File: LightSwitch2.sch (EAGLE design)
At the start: 3 parts, among them SW1 SWITCH-SPDT-ILLUMINATED, SW2 SWITCH-SPDT-ILLUMINATED

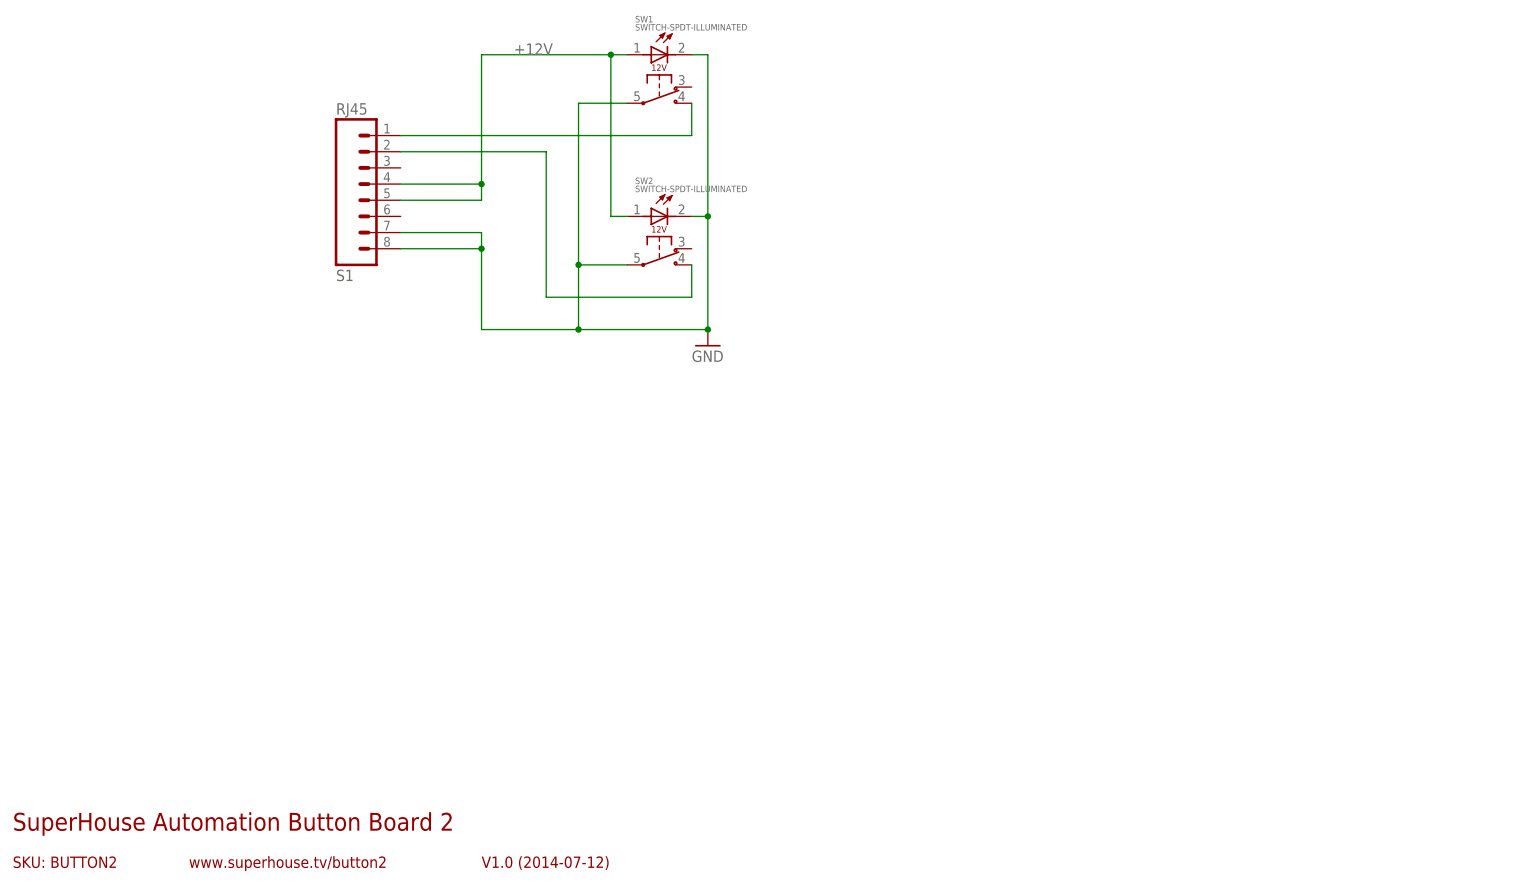
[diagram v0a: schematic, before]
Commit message: Improved labels for clarity
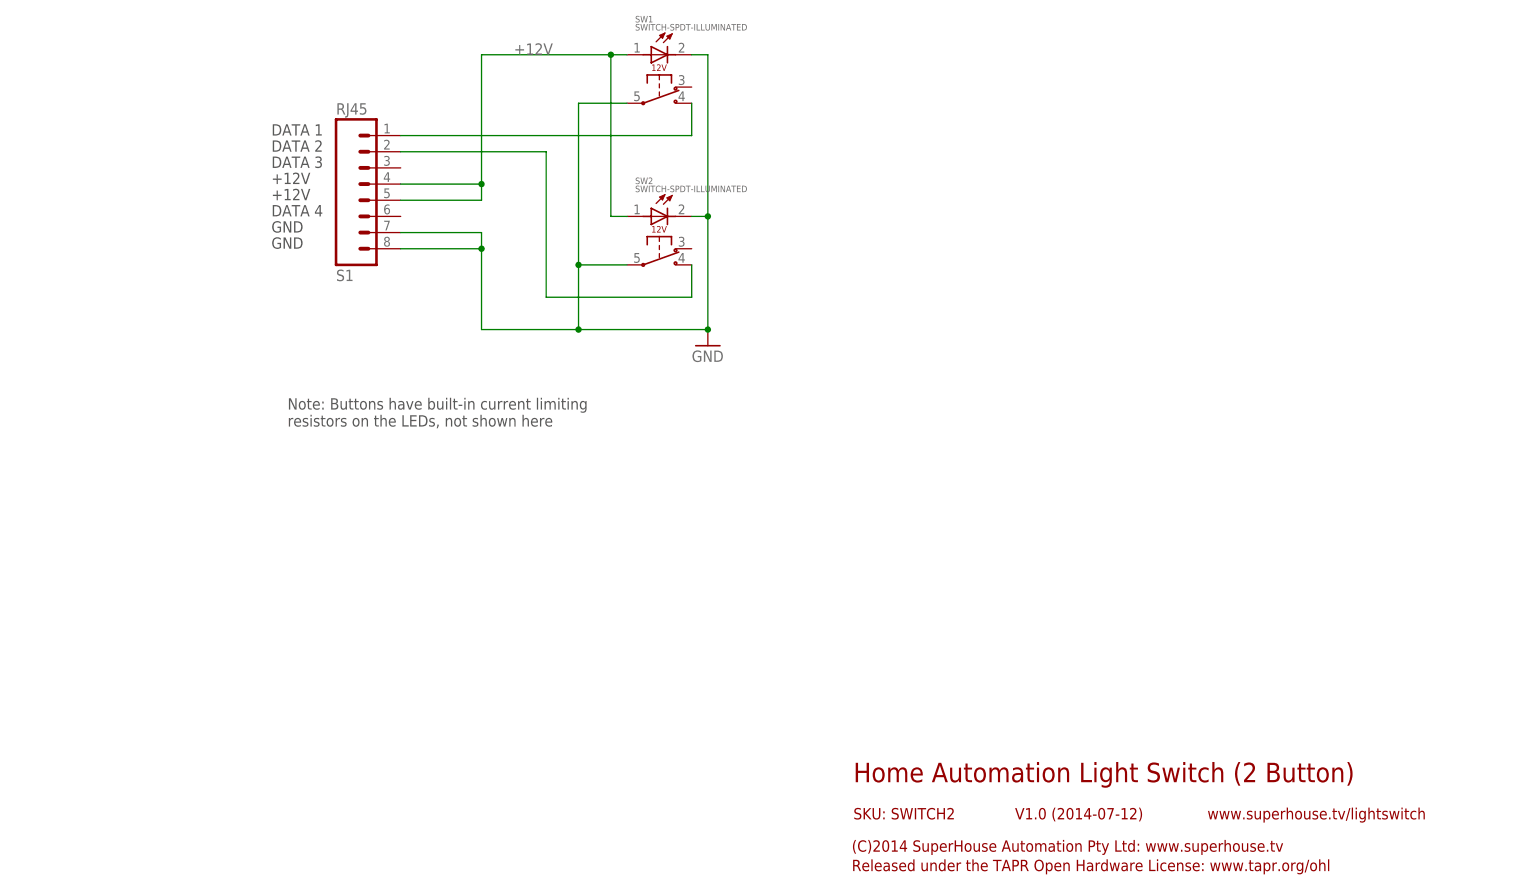
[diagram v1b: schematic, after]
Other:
- note added: "(C)2014 SuperHouse Automation Pty Ltd: www.superhouse.tv"
- note added: "+12V"
- note added: "DATA 1"
- note added: "DATA 2"
- note added: "DATA 3"
- note added: "DATA 4"
- note added: "GND"
- note added: "Home Automation Light Switch (2 Button)"
- note added: "Note: Buttons have built-in current limiting resistors on the LEDs, not shown here"
- note added: "Released under the TAPR Open Hardware License: www.tapr.org/ohl"
- note added: "SKU: SWITCH2"
- note added: "www.superhouse.tv/lightswitch"
- note removed: "SKU: BUTTON2"
- note removed: "SuperHouse Automation Button Board 2"
- note removed: "www.superhouse.tv/button2"
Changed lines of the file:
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@@
 <?xml version="1.0" encoding="utf-8"?>
 <!DOCTYPE eagle SYSTEM "eagle.dtd">
-<eagle version="6.5.0">
+<eagle version="8.3.2">
 <drawing>
 <settings>
 <setting alwaysvectorfont="yes"/>
+<setting keepoldvectorfont="yes"/>
 <setting verticaltext="up"/>
 </settings>
@@
 <sheet>
 <plain>
-<text x="7.62" y="6.858" size="1.778" layer="94">SKU: BUTTON2</text>
-<text x="7.62" y="12.7" size="2.794" layer="94">SuperHouse Automation Button Board 2</text>
-<text x="81.28" y="6.858" size="1.778" layer="94">V1.0 (2014-07-12)</text>
-<text x="35.306" y="6.858" size="1.778" layer="94">www.superhouse.tv/button2</text>
 <frame x1="0" y1="0" x2="248.92" y2="185.42" columns="8" rows="5" layer="94"/>
-<frame x1="5.08" y1="5.08" x2="109.22" y2="17.78" columns="0" rows="0" layer="94" border-left="no" border-top="no" border-right="no" border-bottom="no"/>
-<frame x1="78.74" y1="5.08" x2="109.22" y2="10.16" columns="8" rows="5" layer="94"/>
-<frame x1="5.08" y1="5.08" x2="30.48" y2="10.16" columns="8" rows="5" layer="94"/>
+<text x="139.7" y="20.32" size="3.048" layer="94">Home Automation Light Switch (2 Button)</text>
+<text x="165.1" y="14.478" size="1.778" layer="94">V1.0 (2014-07-12)</text>
+<text x="139.7" y="14.478" size="1.778" layer="94">SKU: SWITCH2</text>
+<text x="139.446" y="9.398" size="1.778" layer="94">(C)2014 SuperHouse Automation Pty Ltd: www.superhouse.tv</text>
+<text x="139.446" y="6.35" size="1.778" layer="94">Released under the TAPR Open Hardware License: www.tapr.org/ohl</text>
+<text x="195.326" y="14.478" size="1.778" layer="94">www.superhouse.tv/lightswitch</text>
+<frame x1="137.16" y1="12.7" x2="243.84" y2="25.4" columns="0" rows="0" layer="94" border-left="no" border-top="no" border-right="no" border-bottom="no"/>
+<frame x1="162.56" y1="12.7" x2="193.04" y2="17.78" columns="8" rows="5" layer="94"/>
+<frame x1="137.16" y1="5.08" x2="243.84" y2="17.78" columns="0" rows="0" layer="94" border-left="no" border-top="no" border-right="no" border-bottom="no"/>
+<text x="48.26" y="121.92" size="1.778" layer="97">DATA 1</text>
+<text x="48.26" y="119.38" size="1.778" layer="97">DATA 2</text>
+<text x="48.26" y="116.84" size="1.778" layer="97">DATA 3</text>
+<text x="48.26" y="109.22" size="1.778" layer="97">DATA 4</text>
+<text x="48.26" y="114.3" size="1.778" layer="97">+12V</text>
+<text x="48.26" y="111.76" size="1.778" layer="97">+12V</text>
+<text x="48.26" y="106.68" size="1.778" layer="97">GND</text>
+<text x="48.26" y="104.14" size="1.778" layer="97">GND</text>
+<text x="50.8" y="76.2" size="1.778" layer="97">Note: Buttons have built-in current limiting
+resistors on the LEDs, not shown here</text>
 </plain>
 <instances>
@@
 </schematic>
 </drawing>
+<compatibility>
+<note version="6.3" minversion="6.2.2" severity="warning">
+Since Version 6.2.2 text objects can contain more than one line,
+which will not be processed correctly with this version.
+</note>
+</compatibility>
 </eagle>

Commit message: Replaced buttons with more common SPST type
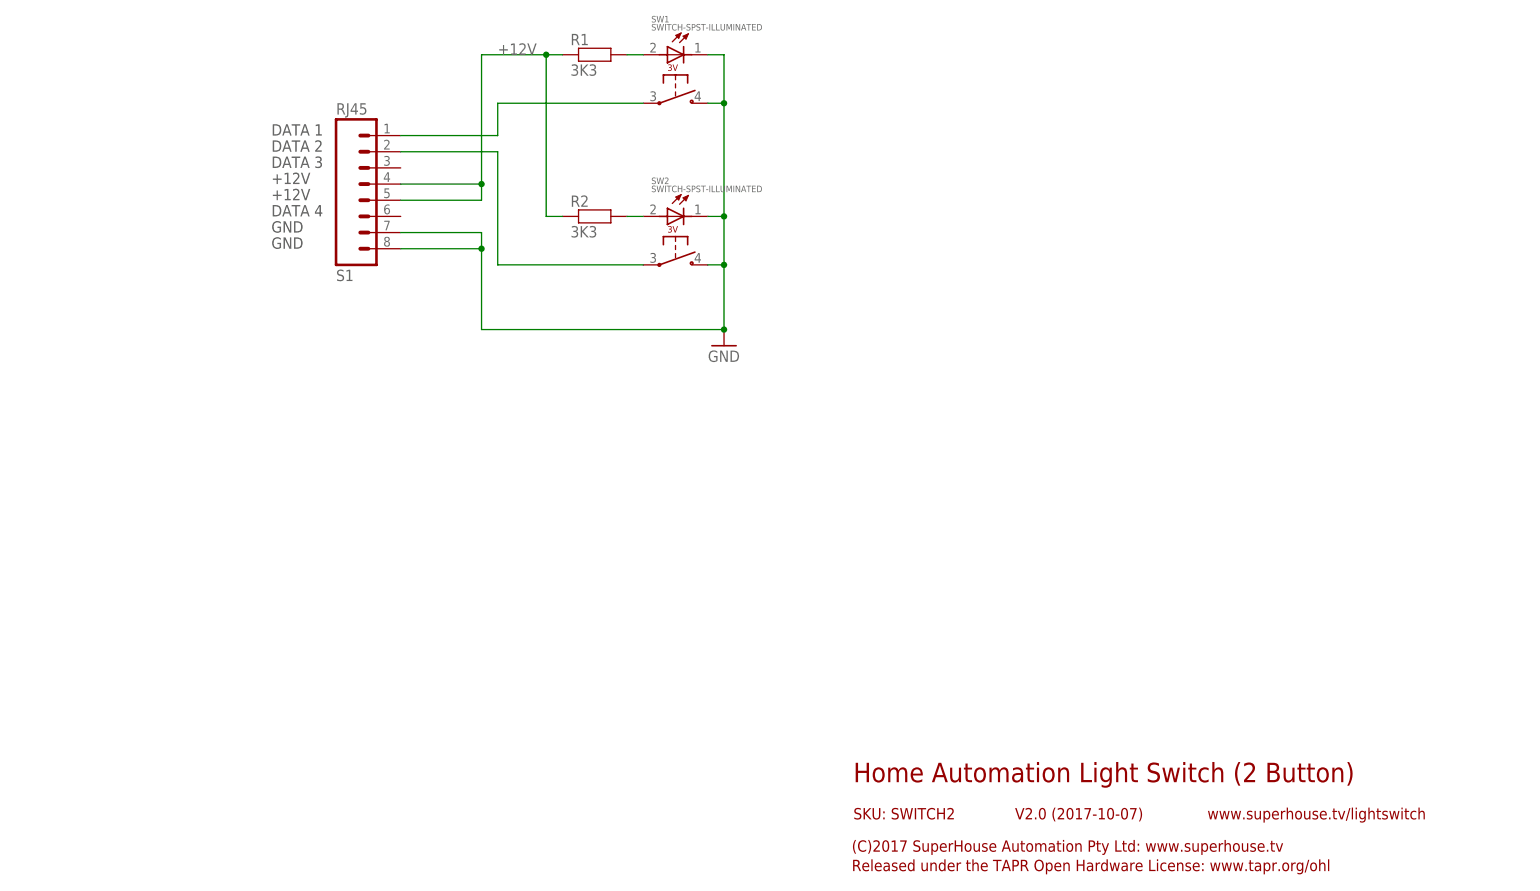
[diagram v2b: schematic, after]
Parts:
- added R1, R2: 3K3, freetronics-jon:RESISTOR0603
- SW1, SW2: value SWITCH-SPDT-ILLUMINATED -> SWITCH-SPST-ILLUMINATED; device freetronics-jon:SWITCH-SPDT-ILLUMINATED -> freetronics-jon:SWITCH-SPST-ILLUMINATED
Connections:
- new net N$1: R1.2, SW1.+
- new net N$2: R2.2, SW2.+
- net +12V: now also R1.1, R2.1; no longer SW1.+, SW2.+
- net GND: now also SW1.NO, SW2.NO; no longer SW1.COM, SW2.COM
- net N$4: now also SW1.COM; no longer SW1.NO
- net N$5: now also SW2.COM; no longer SW2.NO
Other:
- note added: "(C)2017 SuperHouse Automation Pty Ltd: www.superhouse.tv"
- note added: "V2.0 (2017-10-07)"
- note removed: "(C)2014 SuperHouse Automation Pty Ltd: www.superhouse.tv"
- note removed: "Note: Buttons have built-in current limiting resistors on the LEDs, not shown here"
- note removed: "V1.0 (2014-07-12)"
